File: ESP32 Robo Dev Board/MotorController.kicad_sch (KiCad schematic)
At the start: 9 parts, among them U201 STSPIN250

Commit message: First Finished Version 0.1.
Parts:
- Cr1: renamed from C_ref201; value 10000 pF -> (none); footprint Capacitor_SMD:C_0805_2012Metric -> (none)
- Rr1: renamed from R_ref201; value 750 KΩ -> (none); footprint Resistor_SMD:R_0805_2012Metric -> (none)
- renumbered C201 to C3, C202 to C4, Coff201 to Coff1, Roff201 to Roff1, Roff202 to Roff2, Rsns201 to Rsns1, U201 to U3
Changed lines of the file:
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@@
   (symbol (lib_id "Device:R_Small") (at 166.37 130.81 0) (unit 1)
     (in_bom yes) (on_board yes) (fields_autoplaced)
-    (property "Reference" "Rsns201" (id 0) (at 168.91 129.5399 0)
+    (property "Reference" "Rsns1" (id 0) (at 168.91 129.5399 0)
       (effects (font (size 1.27 1.27)) (justify left))
     )
@@
   (symbol (lib_id "Device:C_Small") (at 173.99 82.55 0) (mirror y) (unit 1)
     (in_bom yes) (on_board yes)
-    (property "Reference" "C202" (id 0) (at 180.34 81.28 0)
+    (property "Reference" "C4" (id 0) (at 180.34 81.28 0)
       (effects (font (size 1.27 1.27)) (justify left))
     )
@@
   (symbol (lib_id "power:+3.3V") (at 148.59 76.2 0) (mirror y) (unit 1)
     (in_bom yes) (on_board yes)
-    (property "Reference" "#PWR0205" (id 0) (at 148.59 80.01 0)
+    (property "Reference" "#PWR017" (id 0) (at 148.59 80.01 0)
       (effects (font (size 1.27 1.27)) hide)
     )
@@
   (symbol (lib_id "power:GND") (at 162.56 85.09 0) (mirror y) (unit 1)
     (in_bom yes) (on_board yes) (fields_autoplaced)
-    (property "Reference" "#PWR0207" (id 0) (at 162.56 91.44 0)
+    (property "Reference" "#PWR019" (id 0) (at 162.56 91.44 0)
       (effects (font (size 1.27 1.27)) hide)
     )
@@
   (symbol (lib_id "power:GND") (at 128.27 144.78 0) (unit 1)
     (in_bom yes) (on_board yes) (fields_autoplaced)
-    (property "Reference" "#PWR0204" (id 0) (at 128.27 151.13 0)
+    (property "Reference" "#PWR016" (id 0) (at 128.27 151.13 0)
       (effects (font (size 1.27 1.27)) hide)
     )
@@
   (symbol (lib_id "Device:R_Small") (at 132.08 137.16 0) (unit 1)
     (in_bom yes) (on_board yes)
-    (property "Reference" "Roff202" (id 0) (at 133.35 135.89 0)
+    (property "Reference" "Roff2" (id 0) (at 133.35 135.89 0)
       (effects (font (size 1.27 1.27)) (justify left))
     )
@@
   (symbol (lib_id "Amoskeag-KiCAD-Lib:STSPIN250") (at 148.59 95.25 0) (unit 1)
     (in_bom yes) (on_board yes) (fields_autoplaced)
-    (property "Reference" "U201" (id 0) (at 150.6094 92.71 0)
+    (property "Reference" "U3" (id 0) (at 150.6094 92.71 0)
       (effects (font (size 1.27 1.27)) (justify left))
     )
@@
   (symbol (lib_id "power:GND") (at 114.3 124.46 0) (unit 1)
     (in_bom yes) (on_board yes) (fields_autoplaced)
-    (property "Reference" "#PWR0203" (id 0) (at 114.3 130.81 0)
+    (property "Reference" "#PWR015" (id 0) (at 114.3 130.81 0)
       (effects (font (size 1.27 1.27)) hide)
     )
@@
   (symbol (lib_id "Device:R_Small") (at 128.27 137.16 0) (unit 1)
     (in_bom yes) (on_board yes)
-    (property "Reference" "Roff201" (id 0) (at 119.38 134.62 0)
+    (property "Reference" "Roff1" (id 0) (at 119.38 134.62 0)
       (effects (font (size 1.27 1.27)) (justify left))
     )
@@
   (symbol (lib_id "Device:C_Polarized_Small") (at 162.56 82.55 0) (mirror x) (unit 1)
     (in_bom yes) (on_board yes) (fields_autoplaced)
-    (property "Reference" "C201" (id 0) (at 160.02 81.826 0)
+    (property "Reference" "C3" (id 0) (at 160.02 81.826 0)
       (effects (font (size 1.27 1.27)) (justify right))
     )
@@
   (symbol (lib_id "Device:R_Small") (at 107.95 116.84 90) (unit 1)
     (in_bom yes) (on_board yes)
-    (property "Reference" "R_ref201" (id 0) (at 107.95 119.38 90))
-    (property "Value" "750 KΩ" (id 1) (at 107.95 114.3 90))
-    (property "Footprint" "Resistor_SMD:R_0805_2012Metric" (id 2) (at 107.95 116.84 0)
+    (property "Reference" "Rr1" (id 0) (at 107.95 119.38 90))
+    (property "Value" "" (id 1) (at 107.95 114.3 90))
+    (property "Footprint" "" (id 2) (at 107.95 116.84 0)
       (effects (font (size 1.27 1.27)) hide)
     )
@@
   (symbol (lib_id "power:GND") (at 148.59 144.78 0) (unit 1)
     (in_bom yes) (on_board yes) (fields_autoplaced)
-    (property "Reference" "#PWR0206" (id 0) (at 148.59 151.13 0)
+    (property "Reference" "#PWR018" (id 0) (at 148.59 151.13 0)
       (effects (font (size 1.27 1.27)) hide)
     )
@@
   (symbol (lib_id "Device:C_Small") (at 128.27 142.24 0) (unit 1)
     (in_bom yes) (on_board yes)
-    (property "Reference" "Coff201" (id 0) (at 118.11 142.24 0)
+    (property "Reference" "Coff1" (id 0) (at 118.11 142.24 0)
       (effects (font (size 1.27 1.27)) (justify left))
     )
@@
   (symbol (lib_id "power:GND") (at 166.37 144.78 0) (unit 1)
     (in_bom yes) (on_board yes) (fields_autoplaced)
-    (property "Reference" "#PWR0208" (id 0) (at 166.37 151.13 0)
+    (property "Reference" "#PWR020" (id 0) (at 166.37 151.13 0)
       (effects (font (size 1.27 1.27)) hide)
     )
@@
   (symbol (lib_id "power:GND") (at 173.99 85.09 0) (mirror y) (unit 1)
     (in_bom yes) (on_board yes) (fields_autoplaced)
-    (property "Reference" "#PWR0209" (id 0) (at 173.99 91.44 0)
+    (property "Reference" "#PWR021" (id 0) (at 173.99 91.44 0)
       (effects (font (size 1.27 1.27)) hide)
     )
@@
   (symbol (lib_id "Device:C_Small") (at 114.3 123.19 0) (unit 1)
     (in_bom yes) (on_board yes)
-    (property "Reference" "C_ref201" (id 0) (at 116.84 121.92 0)
-      (effects (font (size 1.27 1.27)) (justify left))
-    )
-    (property "Value" "10000 pF" (id 1) (at 115.57 124.46 0)
-      (effects (font (size 1.27 1.27)) (justify left))
-    )
-    (property "Footprint" "Capacitor_SMD:C_0805_2012Metric" (id 2) (at 114.3 123.19 0)
-      (effects (font (size 1.27 1.27)) hide)
-    )
+    (property "Reference" "Cr1" (id 0) (at 116.84 121.92 0)
+      (effects (font (size 1.27 1.27)) (justify left))
+    )
+    (property "Value" "" (id 1) (at 115.57 124.46 0)
+      (effects (font (size 1.27 1.27)) (justify left))
+    )
+    (property "Footprint" "" (id 2) (at 114.3 123.19 0)
+      (effects (font (size 1.27 1.27)) hide)
+    )

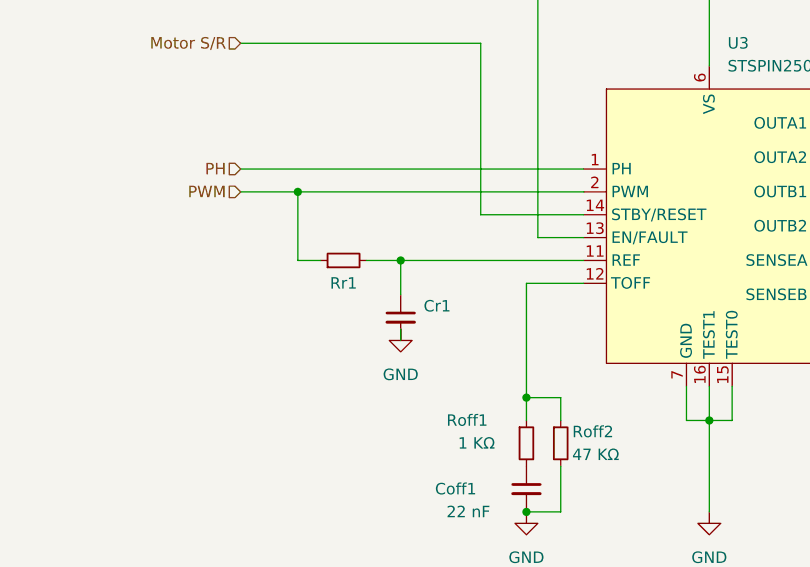
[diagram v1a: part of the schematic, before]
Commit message: Add battery connector
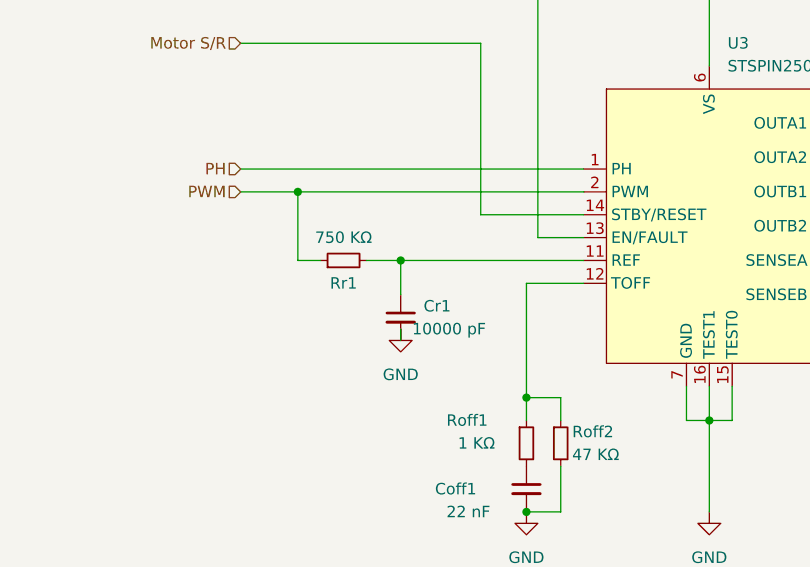
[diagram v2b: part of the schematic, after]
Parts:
- Cr1: value (none) -> 10000 pF; footprint (none) -> Capacitor_SMD:C_0805_2012Metric
- Rr1: value (none) -> 750 KΩ; footprint (none) -> Resistor_SMD:R_0805_2012Metric
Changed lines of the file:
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@@
     (in_bom yes) (on_board yes)
     (property "Reference" "Rr1" (id 0) (at 107.95 119.38 90))
-    (property "Value" "" (id 1) (at 107.95 114.3 90))
-    (property "Footprint" "" (id 2) (at 107.95 116.84 0)
+    (property "Value" "750 KΩ" (id 1) (at 107.95 114.3 90))
+    (property "Footprint" "Resistor_SMD:R_0805_2012Metric" (id 2) (at 107.95 116.84 0)
       (effects (font (size 1.27 1.27)) hide)
     )
@@
       (effects (font (size 1.27 1.27)) (justify left))
     )
-    (property "Value" "" (id 1) (at 115.57 124.46 0)
+    (property "Value" "10000 pF" (id 1) (at 115.57 124.46 0)
       (effects (font (size 1.27 1.27)) (justify left))
     )
-    (property "Footprint" "" (id 2) (at 114.3 123.19 0)
+    (property "Footprint" "Capacitor_SMD:C_0805_2012Metric" (id 2) (at 114.3 123.19 0)
       (effects (font (size 1.27 1.27)) hide)
     )
